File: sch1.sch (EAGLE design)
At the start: 44 parts, among them K1 351, K2 351, K3 351, K4 351, K5 351, K6 351

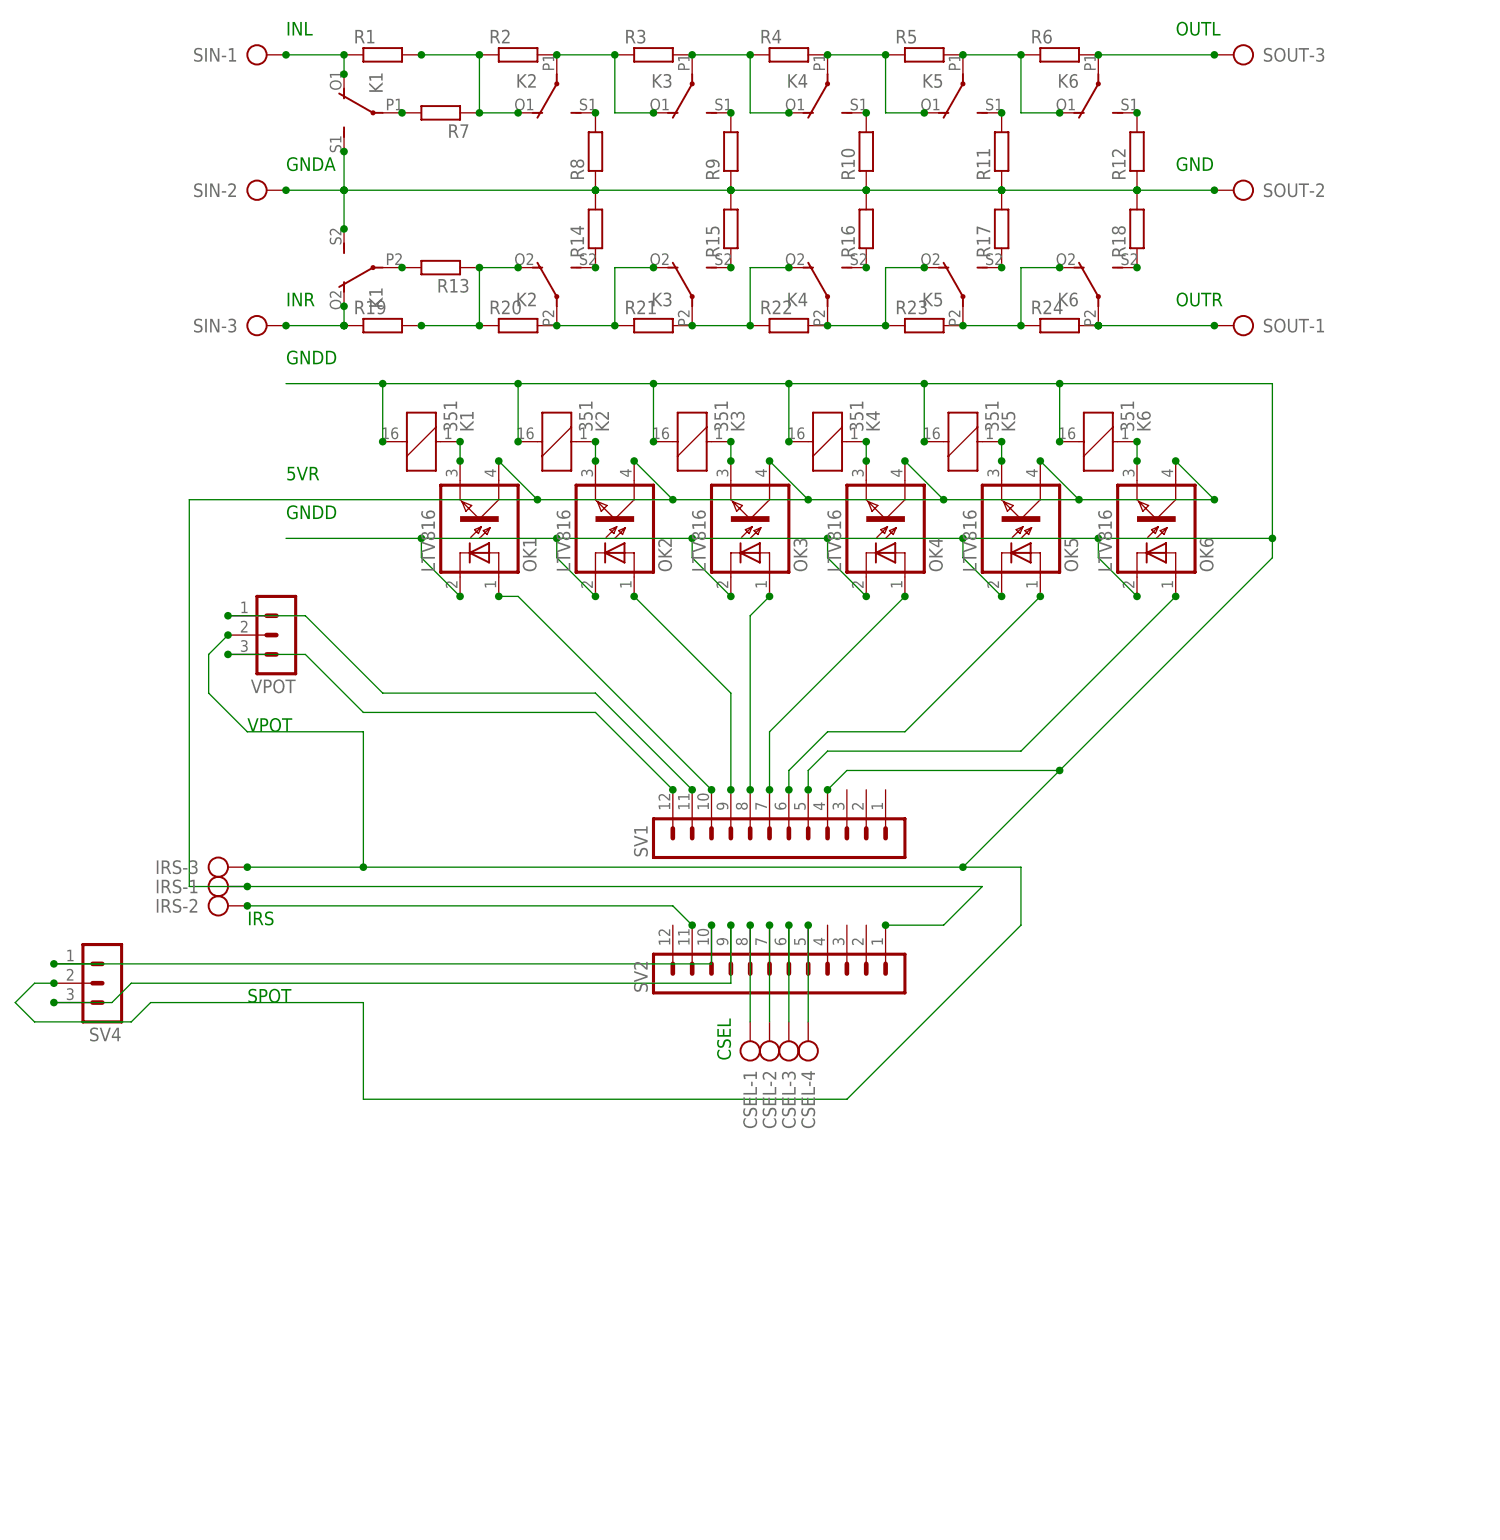
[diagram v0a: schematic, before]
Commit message: added ground fill on bottom
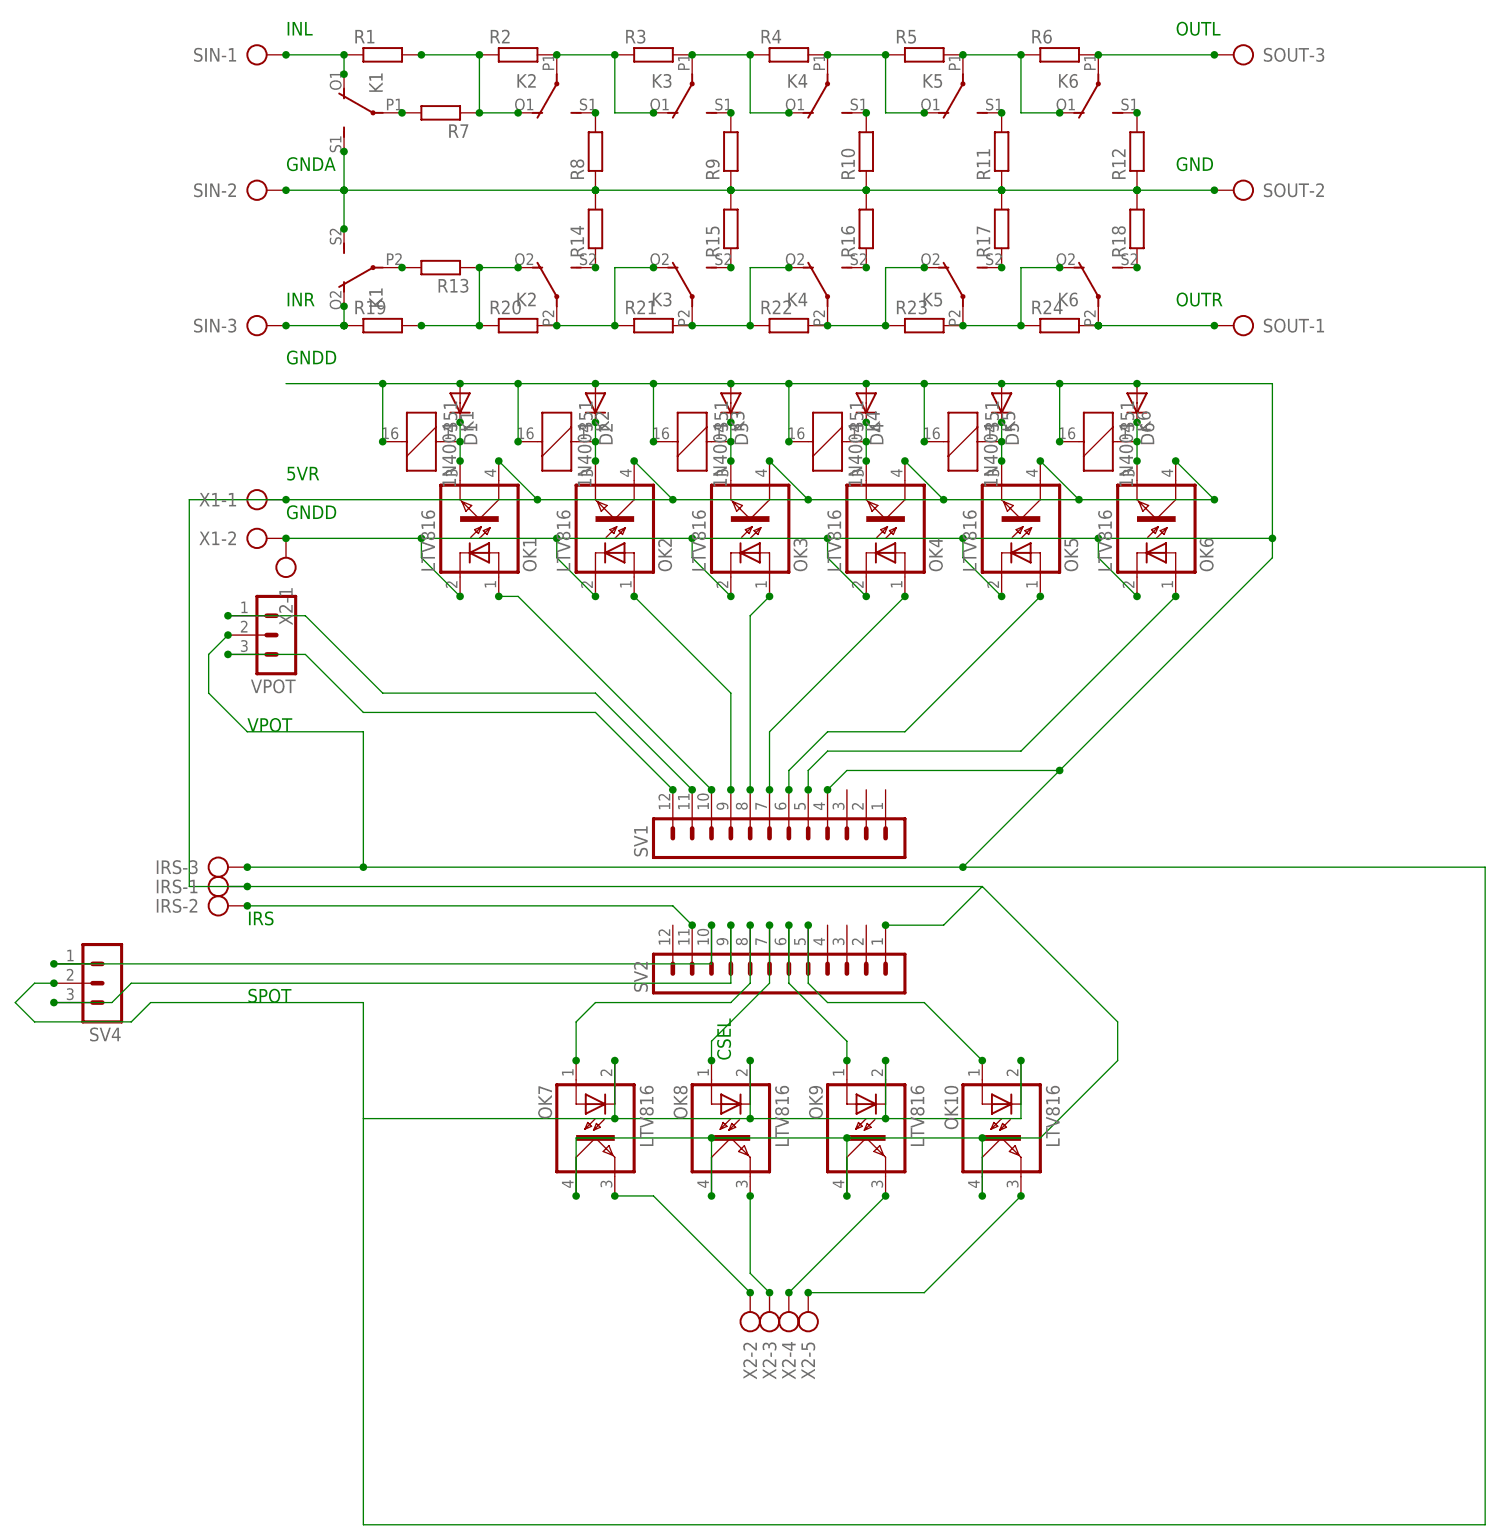
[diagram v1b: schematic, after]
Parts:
- removed CSEL: (no value), con-ptr500:AK500/4
- added D1, D2, D3, D4, D5, D6: 1N4004, diode:1N4004
- added OK10, OK7, OK8, OK9: LTV816, optocoupler:LTV816
- added X1: (no value), con-ptr500:AK500/2
- added X2: (no value), con-ptr500:AK500/5
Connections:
- new net N$93: OK7.EMIT, X2-2.KL
- new net N$94: OK8.EMIT, X2-3.KL
- new net N$95: OK9.EMIT, X2-4.KL
- new net N$96: OK10.EMIT, X2-5.KL
- net GNDD: now also D1.A, D2.A, D3.A, D4.A, D5.A, D6.A, OK10.C, OK7.C, OK8.C, OK9.C, X1-2.KL, X2-1.KL
- net N$21: now also OK7.A; no longer CSEL-1.KL
- net N$23: now also D1.C
- net N$24: now also D2.C
- net N$25: now also D3.C
- net N$26: now also D4.C
- net N$27: now also D5.C
- net N$33: now also D6.C
- net N$44: now also OK8.A; no longer CSEL-2.KL
- net N$45: now also OK9.A; no longer CSEL-3.KL
- net N$46: now also OK10.A; no longer CSEL-4.KL
- net N$50: now also OK10.COL, OK7.COL, OK8.COL, OK9.COL, X1-1.KL
